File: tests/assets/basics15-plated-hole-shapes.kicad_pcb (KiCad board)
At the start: 2 copper layers, 30 x 50 mm, 4 parts

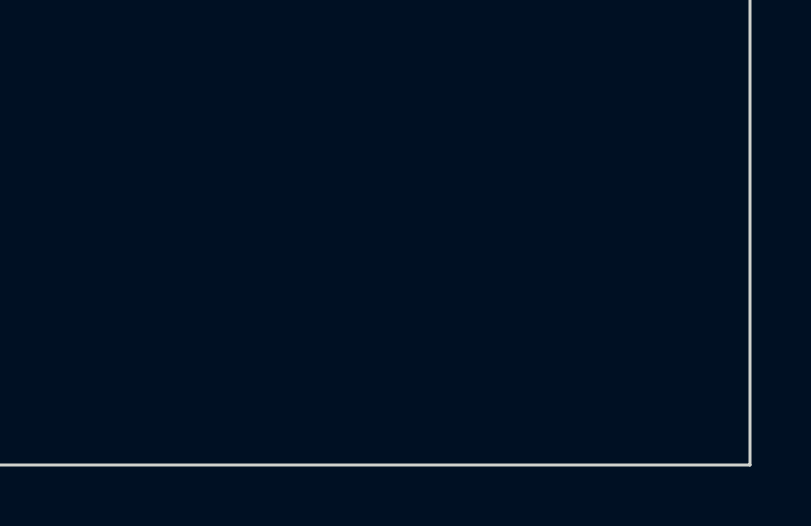
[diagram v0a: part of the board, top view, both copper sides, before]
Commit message: feat: implement rotation support for circular_hole_with_rect_pad and rotated_pill_hole_with_rect_pad
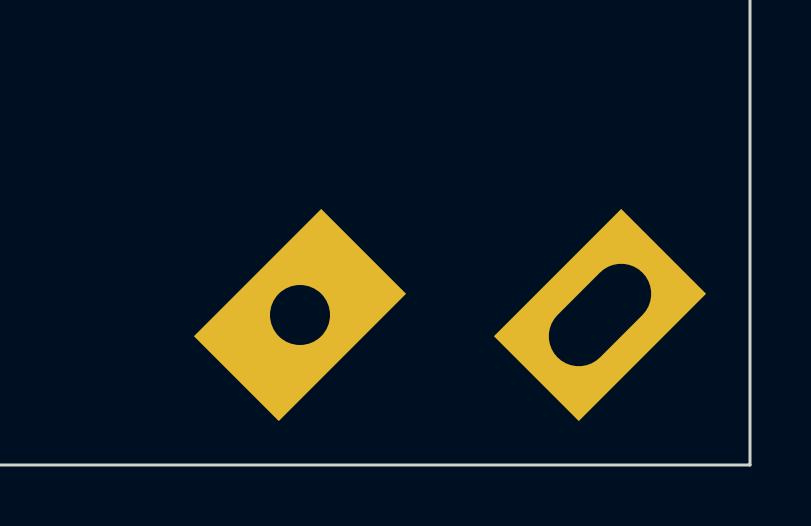
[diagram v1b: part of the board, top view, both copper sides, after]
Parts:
- added ?: , tscircuit:platedhole_circular_hole_with_rect_pad_holeDiameter2mm_rectPadWidth6mm_rectPadHeight4mm_ccwRotation45deg, F.Cu at (100.0, 120.0)
- added ?: , tscircuit:platedhole_rotated_pill_hole_with_rect_pad_holeWidth4mm_holeHeight2mm_rectPadWidth6mm_rectPadHeight4mm_ccwRot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, F.Cu at (110.0, 120.0)
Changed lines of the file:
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@@
+    )
+  )
+  (footprint
+    "tscircuit:platedhole_circular_hole_with_rect_pad_holeDiameter2mm_rectPadWidth6mm_rectPadHeight4mm_ccwRotation45deg"
+    (layer F.Cu)
+    (at 100 120 0)
+    (pad "1" thru_hole rect
+      (at 0 0 45)
+      (size 6 4)
+      (drill 2)
+      (layers *.Cu *.Mask)
+    )
+  )
+  (footprint
+    "tscircuit:platedhole_rotated_pill_hole_with_rect_pad_holeWidth4mm_holeHeight2mm_rectPadWidth6mm_rectPadHeight4mm_ccwRotation45deg"
+    (layer F.Cu)
+    (at 110 120 0)
+    (pad "1" thru_hole rect
+      (at 0 0 45)
+      (size 6 4)
+      (drill oval 4 2)
+      (layers *.Cu *.Mask)
     )
   )
